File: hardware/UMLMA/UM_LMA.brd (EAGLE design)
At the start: 17.8 x 16.8 mm, 14 parts, among them IC1 TINY25, J1 AVRISP6_TP

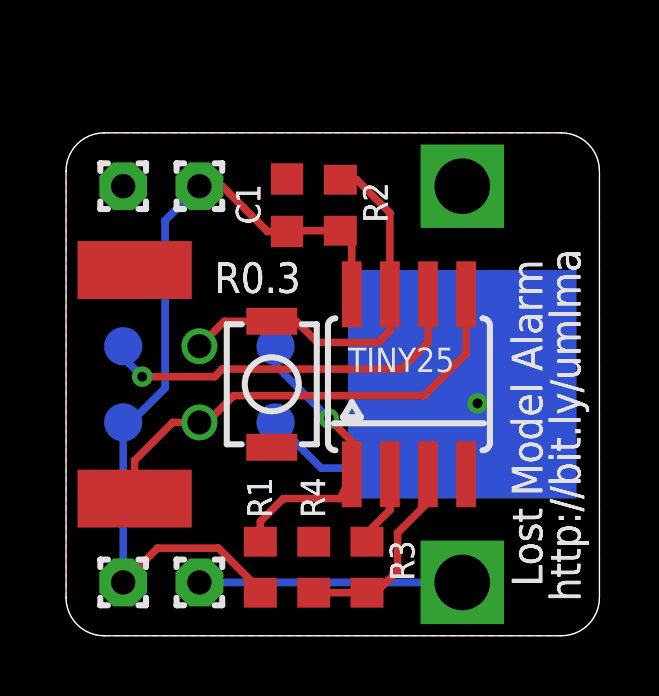
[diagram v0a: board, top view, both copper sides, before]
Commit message: fixed batt/isp interference, revised layout again, revised board size, modified silk
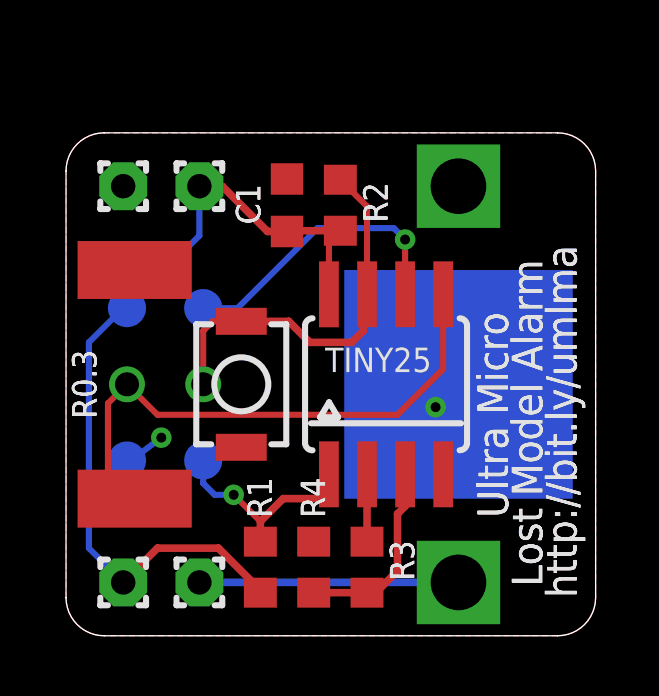
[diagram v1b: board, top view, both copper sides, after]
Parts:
- moved J1 1.14 mm to (3.30, 8.38), turned to 0 degrees
- moved S1 1.02 mm to (5.84, 8.38)
- moved IC1 0.76 mm to (10.7, 8.38)
- moved BAT 0.13 mm to (13.1, 8.38)
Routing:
- net GND: track 8.92 -> 2.47 mm, vias 1 -> 2
- net MISO: track 12.9 -> 9.82 mm
- net MOSI: track 15.8 -> 18.5 mm
- net !RESET: track 9.87 -> 7.28 mm
- net VCC: track 27.7 -> 28.6 mm
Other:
- board size 17.8 x 16.8 mm -> 17.7 x 16.8 mm
- board text added: "Ultra Micro"

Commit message: revised to fix silk conflicts, narrowed silk lines
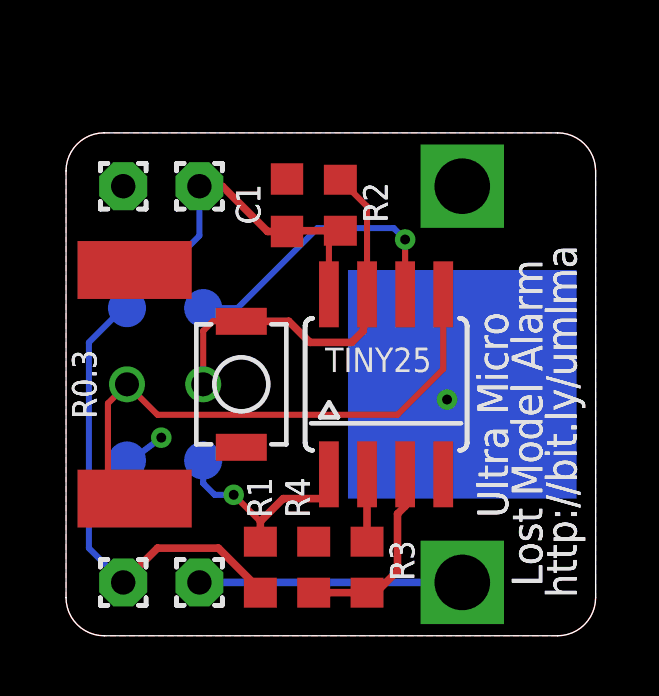
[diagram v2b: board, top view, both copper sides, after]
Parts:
- moved BAT 0.13 mm to (13.2, 8.38)

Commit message: Removed extraneous switch pull-up resistor, moved layout and silk labels, increased switch footprint sizes, updated gerbers
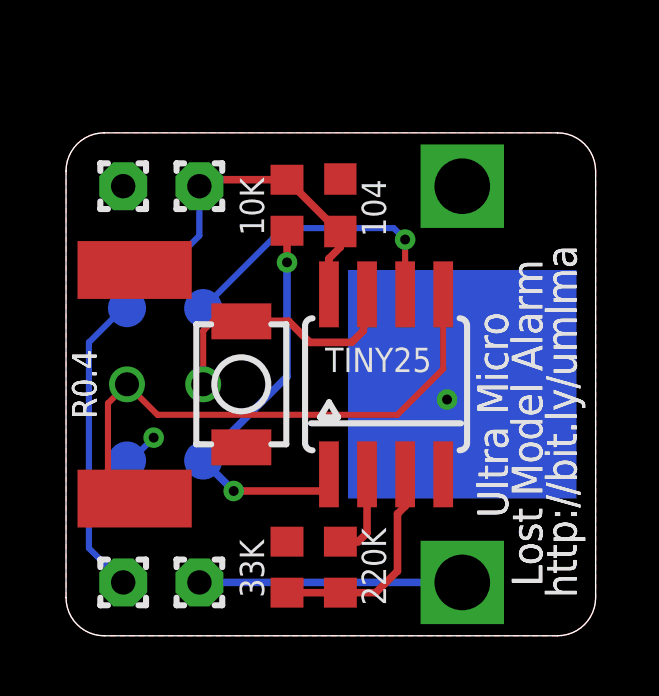
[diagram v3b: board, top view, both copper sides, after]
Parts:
- removed R4: 33K, rcl:R0603
- R2: value 10K -> 220K
- R3: value 220K -> 33K
- moved R1 12.1 mm to (7.37, 14.4), turned to 270 degrees
- moved R2 12.1 mm to (9.14, 2.29), turned to 270 degrees
- moved R3 2.67 mm to (7.37, 2.29), turned to 90 degrees
- moved C1 1.78 mm to (9.14, 14.4)
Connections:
- net GND: now also R3.2; no longer R4.2
- net N$5: now also R2.1; no longer R3.1
- net SCK: no longer R2.2
- net VCC: no longer R2.1
- net VTEST: now also R2.2, R3.1; no longer R3.2, R4.1
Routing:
- net !RESET: track 7.28 -> 14.0 mm, vias 1 -> 2
- net VCC: track 28.6 -> 23.0 mm
- net SCK: track 13.1 -> 8.92 mm
- net VTEST: track 6.42 -> 7.31 mm
- net N$5: track 2.25 -> 2.96 mm
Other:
- board text added: "104"
- board text added: "10K"
- board text added: "220K"
- board text added: "33K"
- board text added: "R0.4"
- board text removed: "C1"
- board text removed: "R0.3"
- board text removed: "R1"
- board text removed: "R2"
- board text removed: "R3"
- board text removed: "R4"
